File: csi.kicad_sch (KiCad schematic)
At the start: 0 parts

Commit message: feat: refactor schematics - remove Ethernet and M.2 NVMe, compact power entry J4, and integrate CAM_L and CAM_R stereo camera sensors
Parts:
- added C9: C_100n_0402, jetson-footprints:C_0402_1005Metric, symbol jetson-symbols:C_100n_0402
- added C91, C93: 1uF_0402, jetson-footprints:C_0402_1005Metric, symbol jetson-symbols:C_100n_0402
- added C92, C94: 2.2uF_0402, jetson-footprints:C_0402_1005Metric, symbol jetson-symbols:C_100n_0402
- added CAM_L, CAM_R: IMX219_30P, jetson-footprints:Camera_Module_IMX219-D160, symbol jetson-symbols:IMX219_30P
- added J15: Bus_DDR4_SODIMM_CUSTOM_Jetson-Nano-H9.2mm-socket, jetson-footprints:TE_2309413, symbol jetson-symbols:Bus_DDR4_SODIMM_CUSTOM_Jetson-Nano-H9.2mm-socket
- added R122: R_10k_0402, jetson-footprints:R_0402_1005Metric, symbol jetson-symbols:R_10k_0402
- added R13, R15, R17, R19, R21, R57, R58, R59, R60, R61: R_0R_0402, jetson-footprints:R_0402_1005Metric, symbol jetson-symbols:R_0R_0402
- added R34, R35: R_2k_0402, jetson-footprints:R_0402_1005Metric, symbol jetson-symbols:R_2k_0402
- added R69: R_100k_0402, jetson-footprints:R_0402_1005Metric, symbol jetson-symbols:R_100k_0402
- added T8: BSS138PW, jetson-footprints:SC70-3, symbol jetson-symbols:BSS138PW
- added TP1, TP10, TP3, TP4, TP6, TP9: TP_1.5mm_SMD, jetson-footprints:TP_SMD_1.5mm, symbol jetson-symbols:TP_1.5mm_SMD
- added U10: TPS7A0528PDBVR, jetson-footprints:SOT-23-5, symbol jetson-symbols:TPS7A0518P_SOT23-5
- added U11: TPS7A0512PDBVR, jetson-footprints:SOT-23-5, symbol jetson-symbols:TPS7A0518P_SOT23-5
- added U4: PCA9547_VQFN, jetson-footprints:VQFN-24-1EP_3.8x3.8x1.0mm_P0.5mm, symbol jetson-symbols:PCA9547_VQFN
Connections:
- new net: J15.11 ((CSI1_CLK)RSVD), J15.9 ((CSI1_CLK)RSVD), TP3.1, TP4.1
- new net: J15.118 (GPIO01), TP9.1
- new net: J15.120 (CAM1_PWDN), TP6.1
- new net: R13.1, U4.1 (SD0)
- new net: R15.1, U4.2 (SC0)
- new net: R17.1, U4.3 (SD1)
- new net: R21.1, U4.4 (SC1)
- new net: R19.1, U4.5 (SD2)
- new net: R58.1, U4.6 (SC2)
- new net: R59.1, U4.7 (SD3)
- new net: R61.1, U4.8 (SC3)
- new net: R57.2, U4.20 (SDA)
- new net: R60.2, U4.19 (SCL)
- new net: R122.2, T8.3 (D), U4.24 (~{RESET})
- new net 1V2_CAM: C94.1, CAM_L.4 (VD1V2), CAM_R.4 (VD1V2), U11.5 (VOUT)
- new net 1V8_SYS: CAM_L.3 (VO1V8), CAM_L.5 (/PWDN), CAM_R.3 (VO1V8), CAM_R.5 (/PWDN)
- new net 2V8_CAM: C92.1, CAM_L.10 (VA2V8), CAM_R.10 (VA2V8), U10.5 (VOUT)
- new net 3V3_SYS: C9.1, C91.1, C93.1, R122.1, R34.1, R35.1, U10.1 (VIN), U10.3 (EN), U11.1 (VIN), U11.3 (EN), U4.21 (VCC)
- new net CAM0_MCLK: CAM_L.7 (MCLK)
- new net CAM0_SCL: CAM_L.29 (SCL), R15.2
- new net CAM0_SDA: CAM_L.30 (SDA), R13.2
- new net CAM1_MCLK: CAM_R.7 (MCLK)
- new net CAM1_SCL: CAM_R.29 (SCL), R21.2
- new net CAM1_SDA: CAM_R.30 (SDA), R17.2
- new net CAM2_SCL: R58.2
- new net CAM2_SDA: R19.2
- new net CAM3_SCL: R61.2
- new net CAM3_SDA: R59.2
- new net CAM_I2C_SCL: J15.213 (CAM_I2C_SCL), R35.2, R60.1, TP10.1
- new net CAM_I2C_SDA: J15.215 (CAM_I2C_SDA), R34.2, R57.1, TP1.1
- new net CSI_A_CLK_N: CAM_L.26 (MCKN), J15.10 (CSI0_CLK_N)
- new net CSI_A_CLK_P: CAM_L.27 (MCKP), J15.12 (CSI0_CLK_P)
- new net CSI_A_D0_N: CAM_L.23 (MD0N), J15.4 (CSI0_D0_N)
- new net CSI_A_D0_P: CAM_L.24 (MD0P), J15.6 (CSI0_D0_P)
- new net CSI_A_D1_N: CAM_L.20 (MD1N), J15.16 (CSI0_D1_N)
- new net CSI_A_D1_P: CAM_L.21 (MD1P), J15.18 (CSI0_D1_P)
- new net CSI_B_D0_N: J15.3 (CSI1_D0_N)
- new net CSI_B_D0_P: J15.5 (CSI1_D0_P)
- new net CSI_B_D1_N: J15.15 (CSI1_D1_N)
- new net CSI_B_D1_P: J15.17 (CSI1_D1_P)
- new net CSI_C_CLK_N: CAM_R.26 (MCKN), J15.52 (CSI4_CLK_N)
- new net CSI_C_CLK_P: CAM_R.27 (MCKP), J15.54 (CSI4_CLK_P)
- new net CSI_C_D0_N: CAM_R.23 (MD0N), J15.46 (CSI4_D0_N)
- new net CSI_C_D0_P: CAM_R.24 (MD0P), J15.48 (CSI4_D0_P)
- new net CSI_C_D1_N: CAM_R.20 (MD1N), J15.58 (CSI4_D1_N)
- new net CSI_C_D1_P: CAM_R.21 (MD1P), J15.60 (CSI4_D1_P)
- new net CSI_D_D0_N: J15.40 (CSI4_D2_N)
- new net CSI_D_D0_P: J15.42 (CSI4_D2_P)
- new net CSI_D_D1_N: J15.64 (CSI4_D3_N)
- new net CSI_D_D1_P: J15.66 (CSI4_D3_P)
- new net CSI_E_CLK_N: J15.28 (CSI2_CLK_N)
- new net CSI_E_CLK_P: J15.30 (CSI2_CLK_P)
- new net CSI_E_D0_N: J15.22 (CSI2_D0_N)
- new net CSI_E_D0_P: J15.24 (CSI2_D0_P)
- new net CSI_E_D1_N: J15.34 (CSI2_D1_N)
- new net CSI_E_D1_P: J15.36 (CSI2_D1_P)
- new net CSI_F_D0_N: J15.21 (CSI3_D0_N)
- new net CSI_F_D0_P: J15.23 (CSI3_D0_P)
- new net CSI_F_D1_N: J15.33 (CSI3_D1_N)
- new net CSI_F_D1_P: J15.35 (CSI3_D1_P)
- new net CSI_G_CLK_N: J15.76 (DSI_CLK_N)
- new net CSI_G_CLK_P: J15.78 (DSI_CLK_P)
- new net CSI_G_D0_N: J15.70 (DSI_D0_N)
- new net CSI_G_D0_P: J15.72 (DSI_D0_P)
- new net CSI_G_D1_N: J15.82 (DSI_D1_N)
- new net CSI_G_D1_P: J15.84 (DSI_D1_P)
- new net GND: C9.2, C91.2, C92.2, C93.2, C94.2, CAM_L.12 (DGND2), CAM_L.15 (DGND1), CAM_L.16 (DGND5), CAM_L.19 (DGND6), CAM_L.22 (DGND7), CAM_L.25 (DGND8), CAM_L.28 (DGND9), CAM_L.6 (DGND4), CAM_L.8 (DGND3), CAM_L.9 (AGND), CAM_L.SH, CAM_R.12 (DGND2), CAM_R.15 (DGND1), CAM_R.16 (DGND5), CAM_R.19 (DGND6), CAM_R.22 (DGND7), CAM_R.25 (DGND8), CAM_R.28 (DGND9), CAM_R.6 (DGND4), CAM_R.8 (DGND3), CAM_R.9 (AGND), CAM_R.SH, R69.2, T8.2 (S), U10.2 (GND), U11.2 (GND), U4.18 (A2), U4.22 (A0), U4.23 (A1), U4.25 (EP), U4.9 (GND)
- new net I2C_MUX_RESET: R69.1, T8.1 (G)
- new net VSYNC_CAM2_1: J15.114 (CAM0_PWDN)
- no-connect marks 0 -> 28
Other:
- note added: "CAM_L_CLK_N"
- note added: "CAM_L_CLK_P"
- note added: "CAM_L_D0_N"
- note added: "CAM_L_D0_P"
- note added: "CAM_L_D1_N"
- note added: "CAM_L_D1_P"
- note added: "CAM_L_D2_N"
- note added: "CAM_L_D2_P"
- note added: "CAM_L_D3_N"
- note added: "CAM_L_D3_P"
- note added: "CAM_L_SCL"
- note added: "CAM_L_SDA"
- note added: "CAM_R_CLK_N"
- note added: "CAM_R_CLK_P"
- note added: "CAM_R_D0_N"
- note added: "CAM_R_D0_P"
- note added: "CAM_R_D1_N"
- note added: "CAM_R_D1_P"
- note added: "CAM_R_D2_N"
- note added: "CAM_R_D2_P"
- note added: "CAM_R_D3_N"
- note added: "CAM_R_D3_P"
- note added: "CAM_R_SCL"
- note added: "CAM_R_SDA"
- note added: "Camera FFC #1"
- note added: "Camera FFC #2"
- note added: "Camera I2C multiplexer"
- note added: "Camera Interfaces"
- note added: "LEFT CAMERA"
- note added: "RIGHT CAMERA"
- note added: "SoM interface"
- note added: "Text"

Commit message: refactor(pcb,sch): remove all 36 test points and prune associated stub tracks
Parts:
- removed TP1, TP10, TP3, TP4, TP6, TP9: TP_1.5mm_SMD, jetson-footprints:TP_SMD_1.5mm, symbol jetson-symbols:TP_1.5mm_SMD

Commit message: csi
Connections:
- no-connect marks 28 -> 31
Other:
- note added: "CAMERA I2C MULTIPLEXER (PCA9547)"
- note added: "DUAL LDO REGULATORS (2.8V / 1.2V)"
- note added: "JETSON SOM CSI HOST INTERFACE"
- note added: "STEREO IMX219 SENSORS (CAM_L / CAM_R)"
- note removed: "CAM_L_CLK_N"
- note removed: "CAM_L_CLK_P"
- note removed: "CAM_L_D0_N"
- note removed: "CAM_L_D0_P"
- note removed: "CAM_L_D1_N"
- note removed: "CAM_L_D1_P"
- note removed: "CAM_L_D2_N"
- note removed: "CAM_L_D2_P"
- note removed: "CAM_L_D3_N"
- note removed: "CAM_L_D3_P"
- note removed: "CAM_L_SCL"
- note removed: "CAM_L_SDA"
- note removed: "CAM_R_CLK_N"
- note removed: "CAM_R_CLK_P"
- note removed: "CAM_R_D0_N"
- note removed: "CAM_R_D0_P"
- note removed: "CAM_R_D1_N"
- note removed: "CAM_R_D1_P"
- note removed: "CAM_R_D2_N"
- note removed: "CAM_R_D2_P"
- note removed: "CAM_R_D3_N"
- note removed: "CAM_R_D3_P"
- note removed: "CAM_R_SCL"
- note removed: "CAM_R_SDA"
- note removed: "Camera FFC #1"
- note removed: "Camera FFC #2"
- note removed: "Camera I2C multiplexer"
- note removed: "LEFT CAMERA"
- note removed: "RIGHT CAMERA"
- note removed: "SoM interface"
- note removed: "Text"
- moved on the sheet: C91, C92, C93, C94, R34, R35

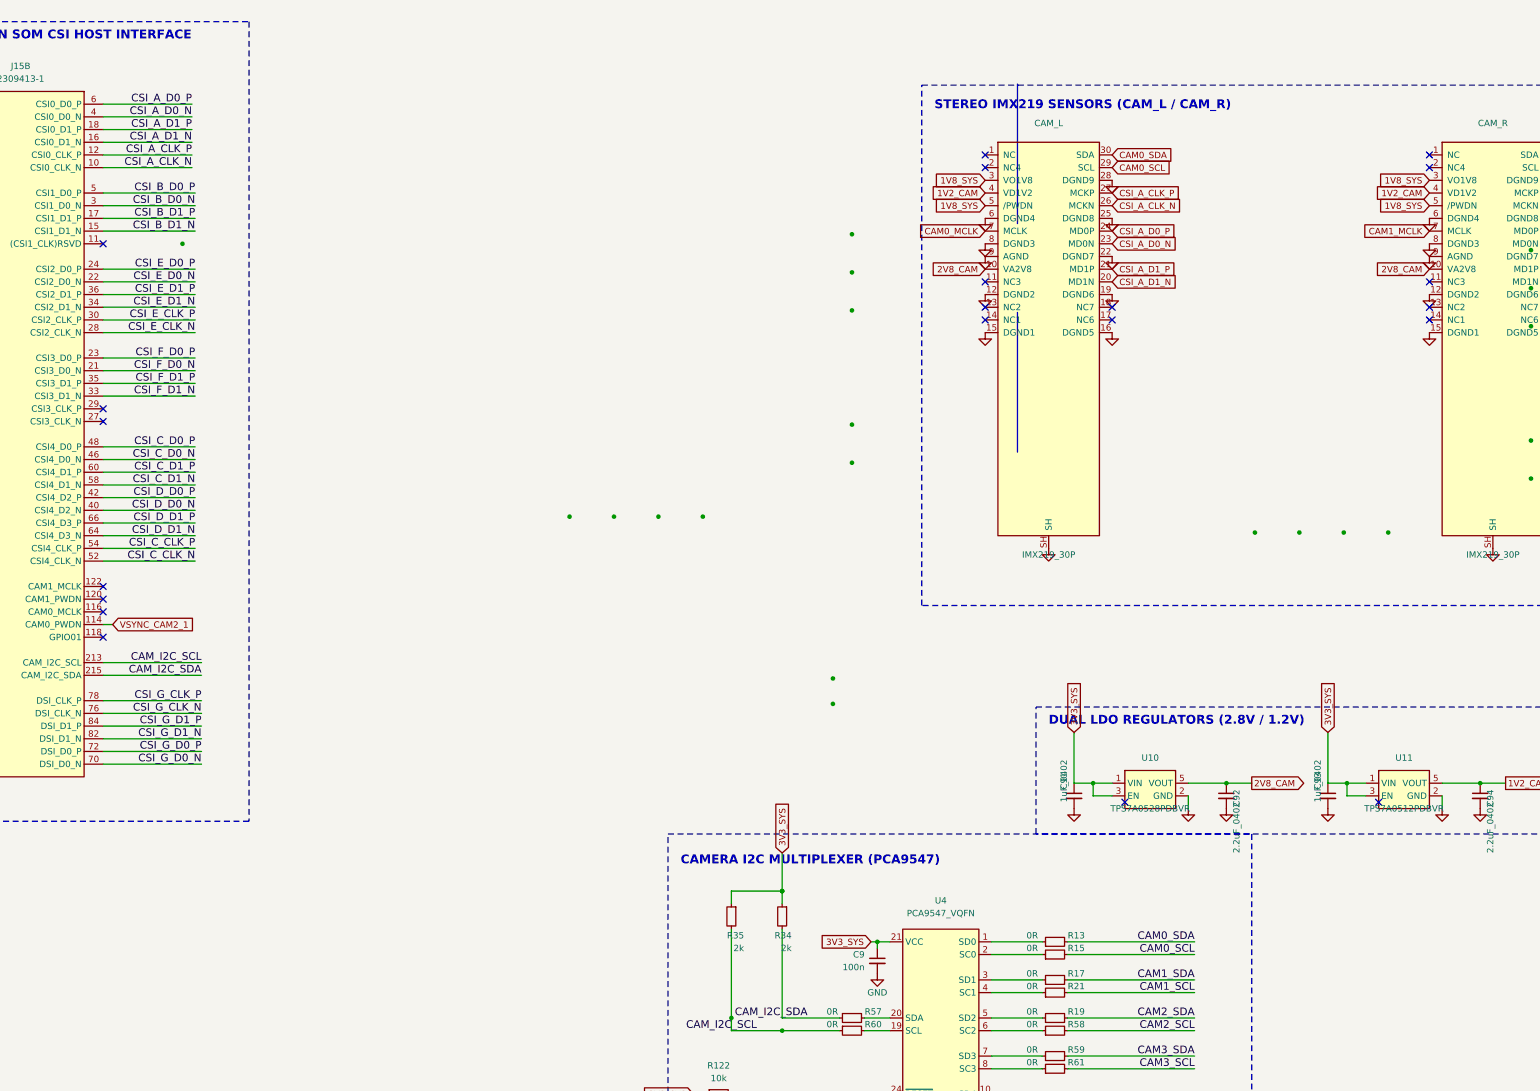
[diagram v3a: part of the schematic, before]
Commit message: fix(schematic): remediate camera clocking, power sequencing, and ERC errors
- Connect Sony IMX219 master clocks (CAM0/1_MCLK) from SoM pins 116/122
- Connect independent PWDN hardware resets from SoM pins 114/120
- Isolate sensor I2C channels (CAM0/1_SCL/SDA) downstream of PCA9547
- Upgrade U11 digital core LDO to TLV75512PDBVR (500mA rating)
- Ground R132 to enable serial EEPROM write-protect
- Connect 3V3_SYS power rail to CAN transceiver U7 and fuse F5
- Eliminate dangling global labels across all sheets
- Configure 25 mil connection grid and achieve 0 ERC errors
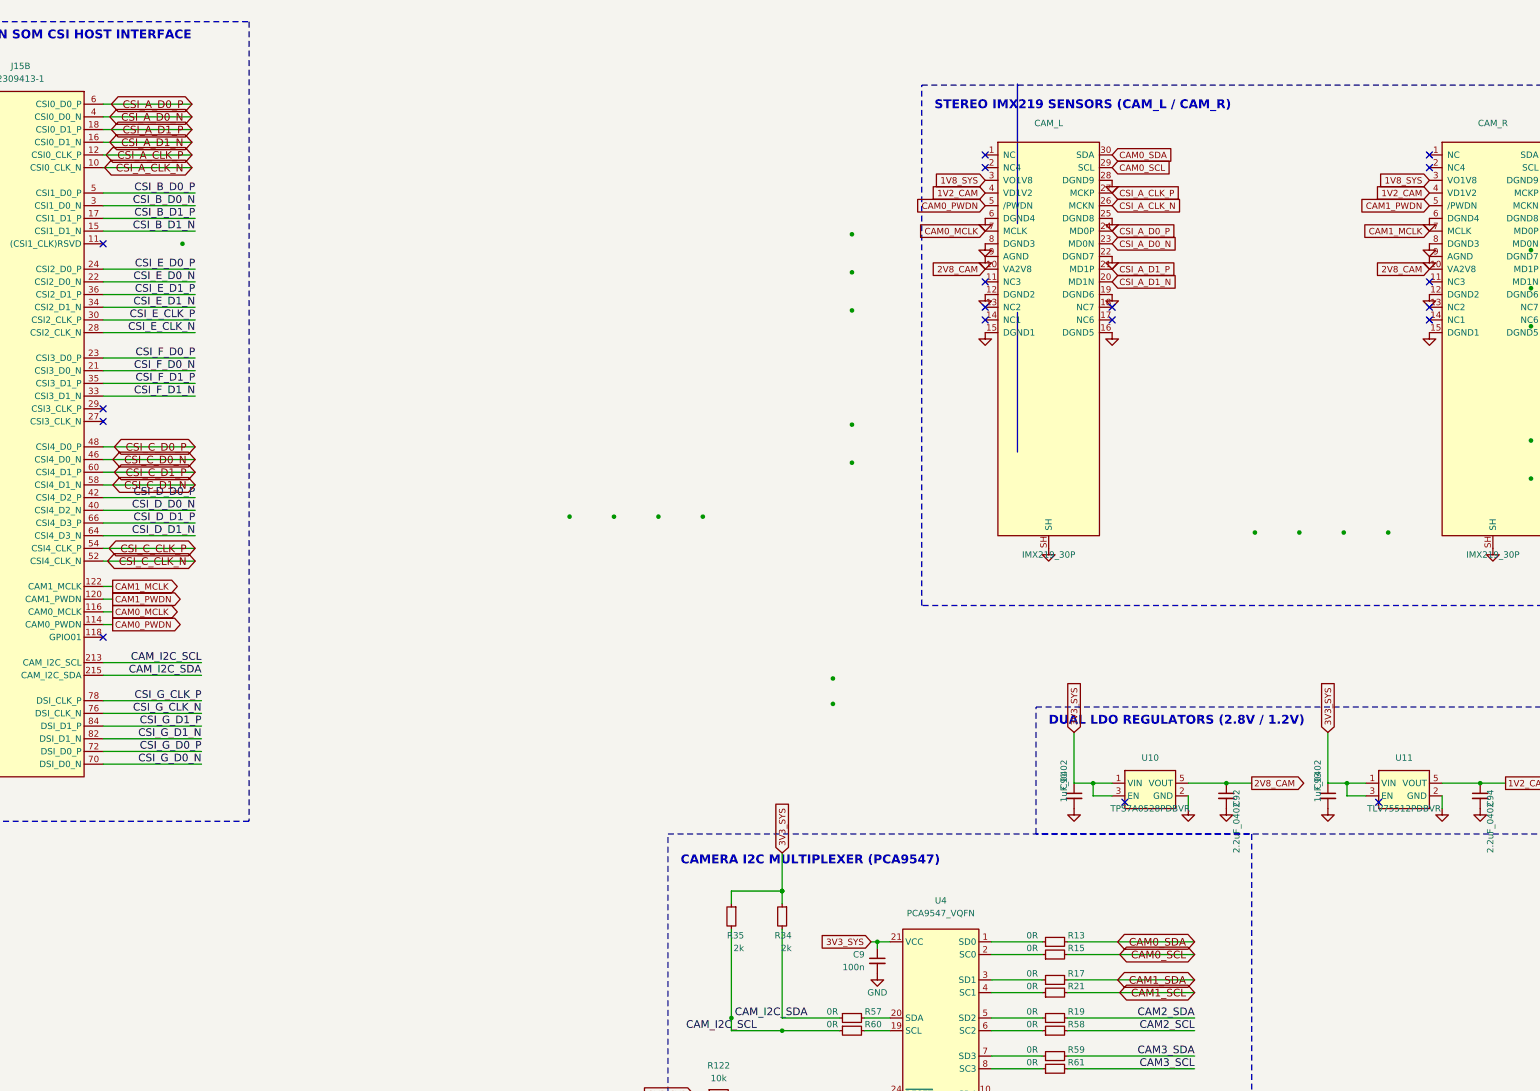
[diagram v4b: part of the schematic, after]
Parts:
- U11: value TPS7A0512PDBVR -> TLV75512PDBVR
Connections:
- net 1V8_SYS: no longer CAM_L.5 (/PWDN), CAM_R.5 (/PWDN)
- net CAM0_MCLK: now also J15.116 (CAM0_MCLK)
- net CAM1_MCLK: now also J15.122 (CAM1_MCLK)
- net CAM1_PWDN: now reaches J15.120 (CAM1_PWDN)
- net CAM1_PWDN: now also CAM_R.5 (/PWDN)
- net VSYNC_CAM2_1 renamed CAM0_PWDN
- net CAM0_PWDN: now also CAM_L.5 (/PWDN)
- no-connect marks 31 -> 28
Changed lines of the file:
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@@
 		)
 	)
-	(label "CSI_A_D1_N"
+	(global_label "CSI_A_D1_N"
+		(shape bidirectional)
 		(at 69.85 49.53 180)
 		(effects
@@
 		)
 	)
-	(label "CSI_A_CLK_P"
+	(global_label "CSI_A_CLK_P"
+		(shape bidirectional)
 		(at 69.85 52.07 180)
 		(effects
@@
 		)
 	)
-	(label "CSI_C_D1_N"
+	(global_label "CSI_C_D1_N"
+		(shape bidirectional)
 		(at 70.485 118.11 180)
 		(effects
@@
 		)
 	)
-	(label "CSI_A_D0_N"
+	(global_label "CSI_A_D0_N"
+		(shape bidirectional)
 		(at 69.85 44.45 180)
 		(effects
@@
 		)
 	)
-	(label "CAM0_SDA"
+	(global_label "CAM0_SDA"
+		(shape bidirectional)
 		(at 270.51 209.55 180)
 		(effects
@@
 		)
 	)
-	(label "CSI_C_CLK_P"
+	(global_label "CSI_C_CLK_P"
+		(shape bidirectional)
 		(at 70.485 130.81 180)
 		(effects
@@
 		)
 	)
-	(label "CAM1_SCL"
+	(global_label "CAM1_SCL"
+		(shape bidirectional)
 		(at 270.51 219.71 180)
 		(effects
@@
 		)
 	)
-	(label "CSI_C_CLK_N"
+	(global_label "CSI_C_CLK_N"
+		(shape bidirectional)
 		(at 70.485 133.35 180)
 		(effects
@@
 		)
 	)
-	(label "CSI_A_D0_P"
+	(global_label "CSI_A_D0_P"
+		(shape bidirectional)
 		(at 69.85 41.91 180)
 		(effects
@@
 		)
 	)
-	(label "CSI_A_D1_P"
+	(global_label "CSI_A_D1_P"
+		(shape bidirectional)
 		(at 69.85 46.99 180)
 		(effects
@@
 		)
 	)
-	(label "CSI_C_D1_P"
+	(global_label "CSI_C_D1_P"
+		(shape bidirectional)
 		(at 70.485 115.57 180)
 		(effects
@@
 		)
 	)
-	(label "CSI_A_CLK_N"
+	(global_label "CSI_A_CLK_N"
+		(shape bidirectional)
 		(at 69.85 54.61 180)
 		(effects
@@
 		)
 	)
-	(label "CSI_C_D0_N"
+	(global_label "CSI_C_D0_N"
+		(shape bidirectional)
 		(at 70.485 113.03 180)
 		(effects
@@
 		)
 	)
-	(label "CAM1_SDA"
+	(global_label "CAM1_SDA"
+		(shape bidirectional)
 		(at 270.51 217.17 180)
 		(effects
@@
 		)
 	)
-	(label "CAM0_SCL"
+	(global_label "CAM0_SCL"
+		(shape bidirectional)
 		(at 270.51 212.09 180)
 		(effects
@@
 		)
 	)
-	(label "CSI_C_D0_P"
+	(global_label "CSI_C_D0_P"
+		(shape bidirectional)
 		(at 70.485 110.49 180)
 		(effects
@@
 		)
 	)
-	(global_label "VSYNC_CAM2_1"
-		(shape input)
+	(global_label "CAM0_PWDN"
+		(shape output)
 		(at 53.975 146.05 0)
 		(fields_autoplaced yes)
@@
 	)	(no_connect
 		(at 229.87 255.27)
-	)	(no_connect
-		(at 52.07 143.51)
-	)	(no_connect
+	)		(no_connect
 		(at 52.07 102.87)
 	)	(no_connect
@@
 	)	(no_connect
 		(at 229.87 250.19)
-	)	(no_connect
-		(at 52.07 138.43)
-	)	(no_connect
+	)		(no_connect
 		(at 52.07 105.41)
 	)	(no_connect
@@
 		)
 	)
-	(global_label "1V8_SYS"
+	(global_label "CAM0_PWDN"
 		(shape input)
 		(at 228.6 62.23 180)
@@
 		)
 	)
-	(global_label "1V8_SYS"
+	(global_label "CAM1_PWDN"
 		(shape input)
 		(at 317.5 62.23 180)
@@
 			(effects (font (size 1.27 1.27)))
 		)
-		(property "Value" "TPS7A0512PDBVR"
+		(property "Value" "TLV75512PDBVR"
 			(at 312.42 182.88000000000002 0)
 			(effects (font (size 1.27 1.27)))
@@
 	)
 	(no_connect
-		(at 52.07 140.97)
-	)
-	(no_connect
 		(at 52.07 148.59)
 	)
@@
 		)
 	)
+	(wire
+		(pts
+			(xy 52.07 143.51) (xy 53.975 143.51)
+		)
+		(stroke
+			(width 0)
+			(type default)
+		)
+	)
+	(global_label "CAM0_MCLK"
+		(shape output)
+		(at 53.975 143.51 0)
+		(fields_autoplaced yes)
+		(effects
+			(font
+				(size 1.27 1.27)
+			)
+			(justify left)
+		)
+	)
+	(wire
+		(pts
+			(xy 52.07 140.97) (xy 53.975 140.97)
+		)
+		(stroke
+			(width 0)
+			(type default)
+		)
+	)
+	(global_label "CAM1_PWDN"
+		(shape output)
+		(at 53.975 140.97 0)
+		(fields_autoplaced yes)
+		(effects
+			(font
+				(size 1.27 1.27)
+			)
+			(justify left)
+		)
+	)
+	(wire
+		(pts
+			(xy 52.07 138.43) (xy 53.975 138.43)
+		)
+		(stroke
+			(width 0)
+			(type default)
+		)
+	)
+	(global_label "CAM1_MCLK"
+		(shape output)
+		(at 53.975 138.43 0)
+		(fields_autoplaced yes)
+		(effects
+			(font
+				(size 1.27 1.27)
+			)
+			(justify left)
+		)
+	)
